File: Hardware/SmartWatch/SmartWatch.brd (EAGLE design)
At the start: 36.8 x 40.6 mm, 55 parts, among them U1 STM32L476, U3 UG-2828GDEDF11, U4 FAN5331SX, U5 APDS-9960, U6 LTC3557

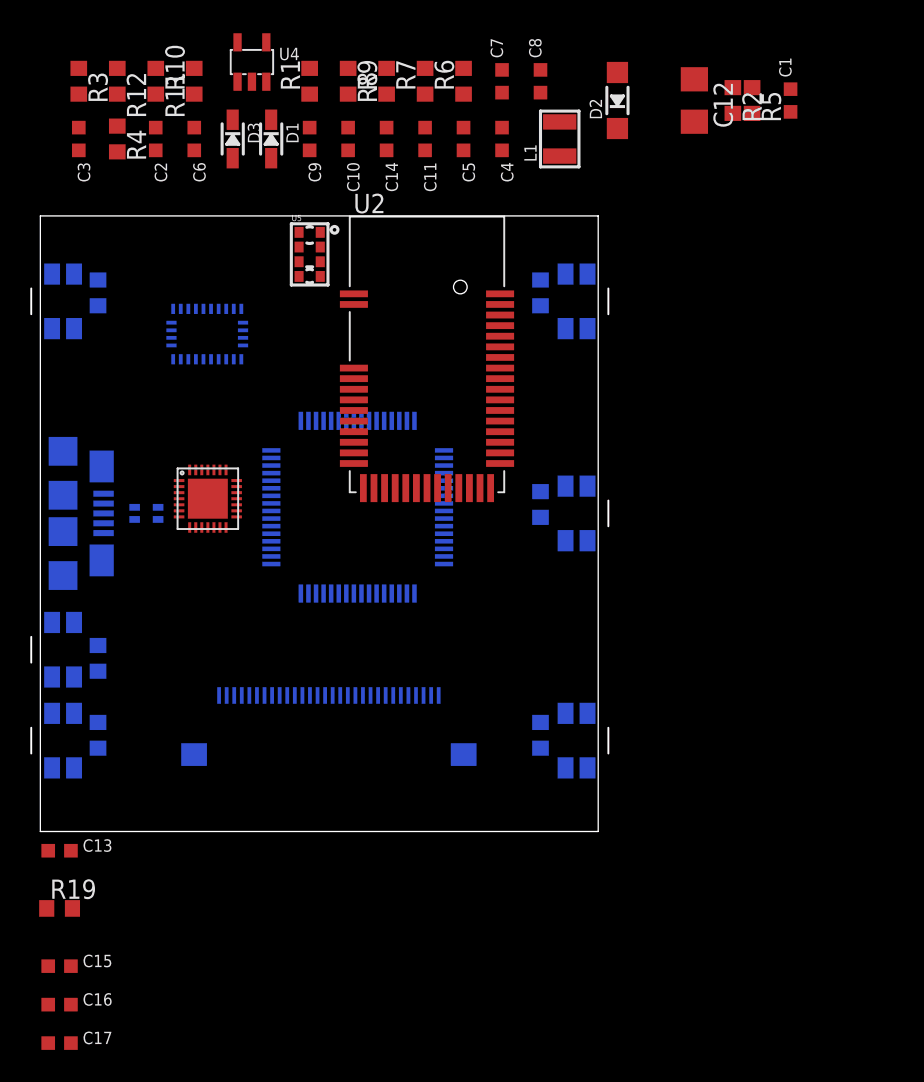
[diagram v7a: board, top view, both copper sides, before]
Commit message: added almost all parts, changed power management IC
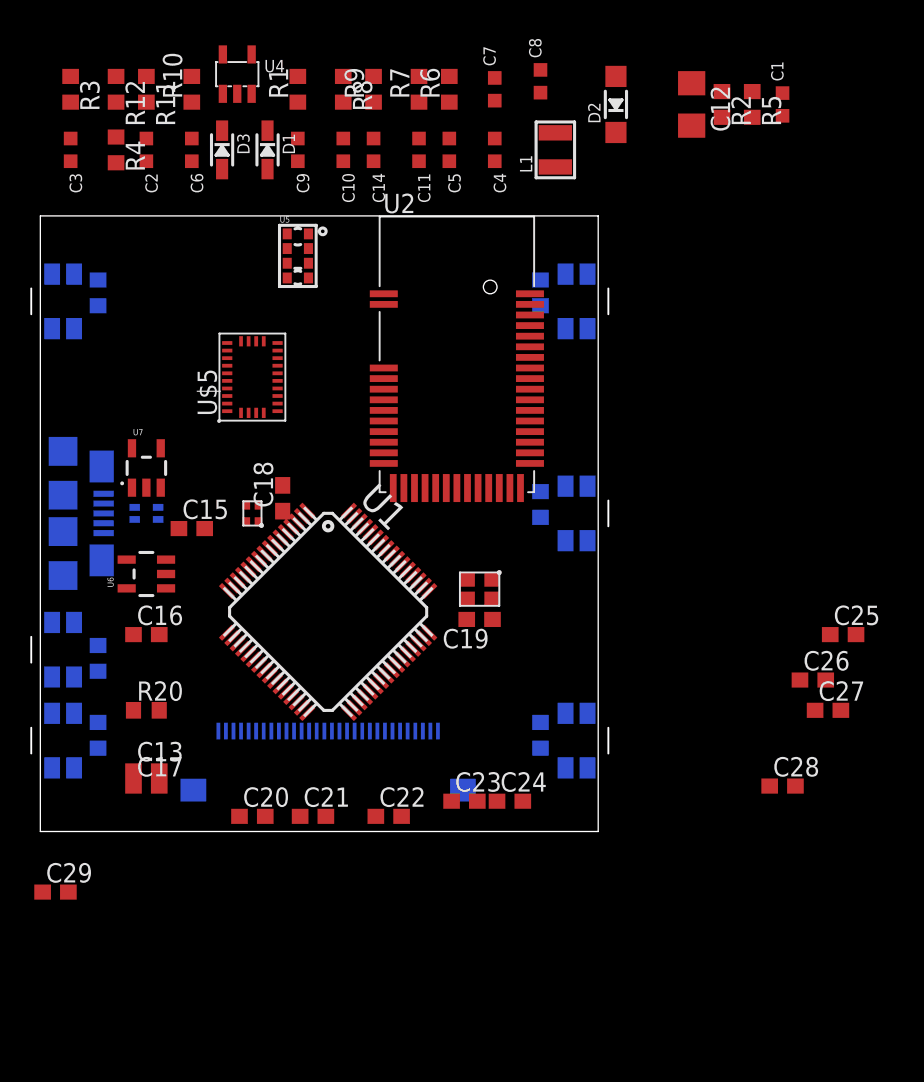
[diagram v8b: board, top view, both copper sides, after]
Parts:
- removed R19: 2.5k, resistor:R0603
- added C18, C19, C20, C21: 1uF, resistor:C0603
- added C22: 0.1nF, resistor:C0603
- added C23, C25, C26: 0.1uF, resistor:C0603
- added C24: 4.7uF, resistor:C0603
- added C27, C28: 2.2uF, resistor:C0603
- added C29: 10nF, resistor:C0603
- added R20: 10K, resistor:R0603
- added U$39: ASCO-8, SmartWatch:ASCO-8
- added U$41: ASDK-32.768, SmartWatch:ASDK-32.768
- added U7: AP2112K-3.3TRG-1, SparkFun-PowerIC:SOT23-5
- C13: value 10uF -> 2.2uF; device microbuilder:0603-MINI -> resistor:C0603
- C15: value 10uF -> 4.7uF; device microbuilder:0603-MINI -> resistor:C0603
- C16: value 2.2uF -> 4.7uF; device microbuilder:0603-MINI -> resistor:C0603
- C17: value 2.2uF -> 1uF; device microbuilder:0603-MINI -> resistor:C0603
- U6: value LTC3557 -> MCP73831; device SmartWatch:28QFN4X4 -> SparkFun:SOT23-5
- moved C15 30.2 mm to (10.0, 20.0)
- moved C16 25.1 mm to (7.00, 13.0)
- moved C17 17.9 mm to (7.00, 3.00)
- moved C13 7.78 mm to (7.00, 4.00)
- moved U1 7.18 mm to (19.0, 14.5), flipped to the top, turned to 315 degrees
- moved U6 6.42 mm to (7.00, 17.0), turned to 90 degrees
- moved U$5 4.12 mm to (14.0, 30.0), flipped to the top, turned to 90 degrees
- moved U3 2.35 mm to (19.0, 4.00)
- moved U2 1.97 mm to (27.5, 31.5)
- moved U4 1.26 mm to (13.0, 50.0)
- moved C5 1.18 mm to (27.0, 45.0)
- moved C14 1.12 mm to (22.0, 45.0)
- moved R6 1.08 mm to (27.0, 49.0)
- moved C9 1.06 mm to (17.0, 45.0)
- moved R9 1.01 mm to (22.0, 49.0)
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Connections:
- removed net BNT_NRST: BTN_NRST.1, BTN_NRST.2, R13.2
- removed net CHRG: U6.28
- removed net N$16: R19.2, U6.20
- removed net N$19: C17.1, U6.6
- removed net N$20: C16.1, U6.16
- removed net VOUT: C15.2, U6.23
- new net BTN_NRST: BTN_NRST.1, BTN_NRST.2, R13.2, U1.7
- new net N$27: C27.1, U1.31
- new net N$29: C28.1, U1.47
- new net OSC32_IN: U$41.3, U1.49
- new net OSC_IN: U$39.1, U1.5
- new net PA0: U1.14
- new net PA1: U1.15
- new net PA10: U1.43
- new net PA13: U1.46
- new net PA14: U1.50
- new net PA2: U1.16
- new net PA3: U1.17
- new net PA4: U1.20
- new net PA5: U1.21
- new net PA6: U1.22
- new net PA7: U1.23
- new net PA8: U1.41
- new net PA9: U1.42
- new net PB0: U1.26
- new net PB1: U1.27
- new net PB10: U1.29
- new net PB11: U1.30
- new net PB12: U1.33
- new net PB13: U1.34
- new net PB14: U1.35
- new net PB15: U1.36
- new net PB2: U1.28
- new net PB3: U1.55
- new net PB4: U1.56
- new net PB5: U1.57
- new net PB6: U1.58
- new net PB7: U1.59
- new net PB8: U1.61
- new net PB9: U1.62
- new net PC0: U1.8
- new net PC1: U1.9
- new net PC10: U1.51
- new net PC11: U1.52
- new net PC12: U1.53
- new net PC13: U1.2
- new net PC14: U1.3
- new net PC15: U1.4
- new net PC2: U1.10
- new net PC3: U1.11
- new net PC4: U1.24
- new net PC5: U1.25
- new net PC6: U1.37
- new net PC7: U1.38
- new net PC8: U1.39
- new net PC9: U1.40
- new net PD2: U1.54
- new net PROG: R20.2, U6.5
- new net STAT: U6.1
- net 3.3V: now also C13.1, C18.1, C19.1, C20.1, C21.1, C22.1, C23.1, C24.1, C25.1, C26.1, C29.1, U$39.4, U$41.4, U1.1, U1.13, U1.19, U1.32, U1.48, U1.64, U7.5
- net BTN_BOOT0: now also U1.60
- net D+: now also U1.45
- net D-: now also U1.44
- net GND: now also C13.2, C15.2, C18.2, C19.2, C20.2, C21.2, C22.2, C23.2, C24.2, C25.2, C26.2, C27.2, C28.2, C29.2, R20.1, U$39.2, U$41.2, U1.12, U1.18, U1.63, U6.2, U7.2, U7.4; no longer C13.1, C15.1, R19.1, U6.19, U6.29
- net N$15: now also U1.6; no longer C13.2, U6.24
- net VBAT: now also C15.1, C17.1, U6.3, U7.1, U7.3; no longer U6.22
- net VUSB: now also C16.1, U6.4
